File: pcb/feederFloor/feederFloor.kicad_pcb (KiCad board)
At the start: 2 copper layers, 13.4 x 31.1 mm, 7 parts, among them J1 IDC, J2 Conn_01x05_Female, U1 DS28E07

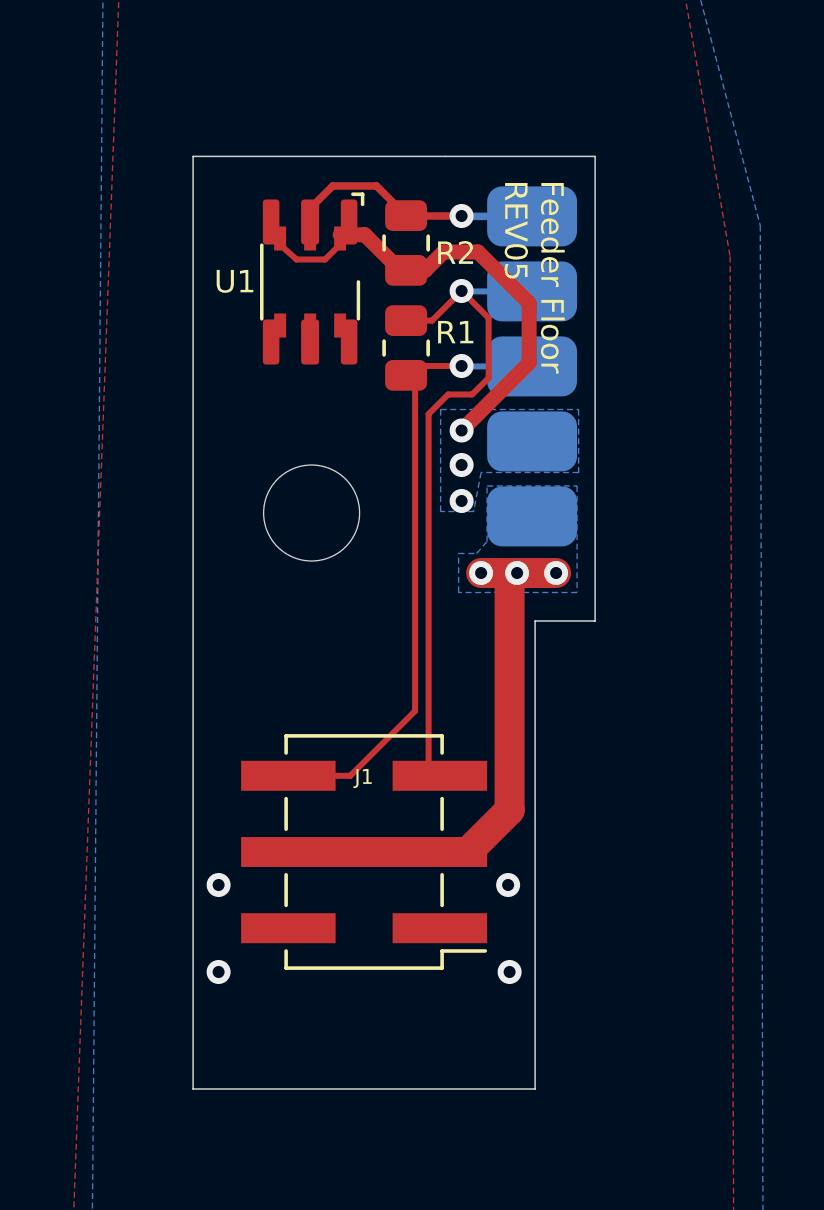
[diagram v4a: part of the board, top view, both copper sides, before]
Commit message: uprevs feederfloor to rev06, through hole IDC connector, adds silk for address, makes pads .1mm thinner, vdc has traces both sides
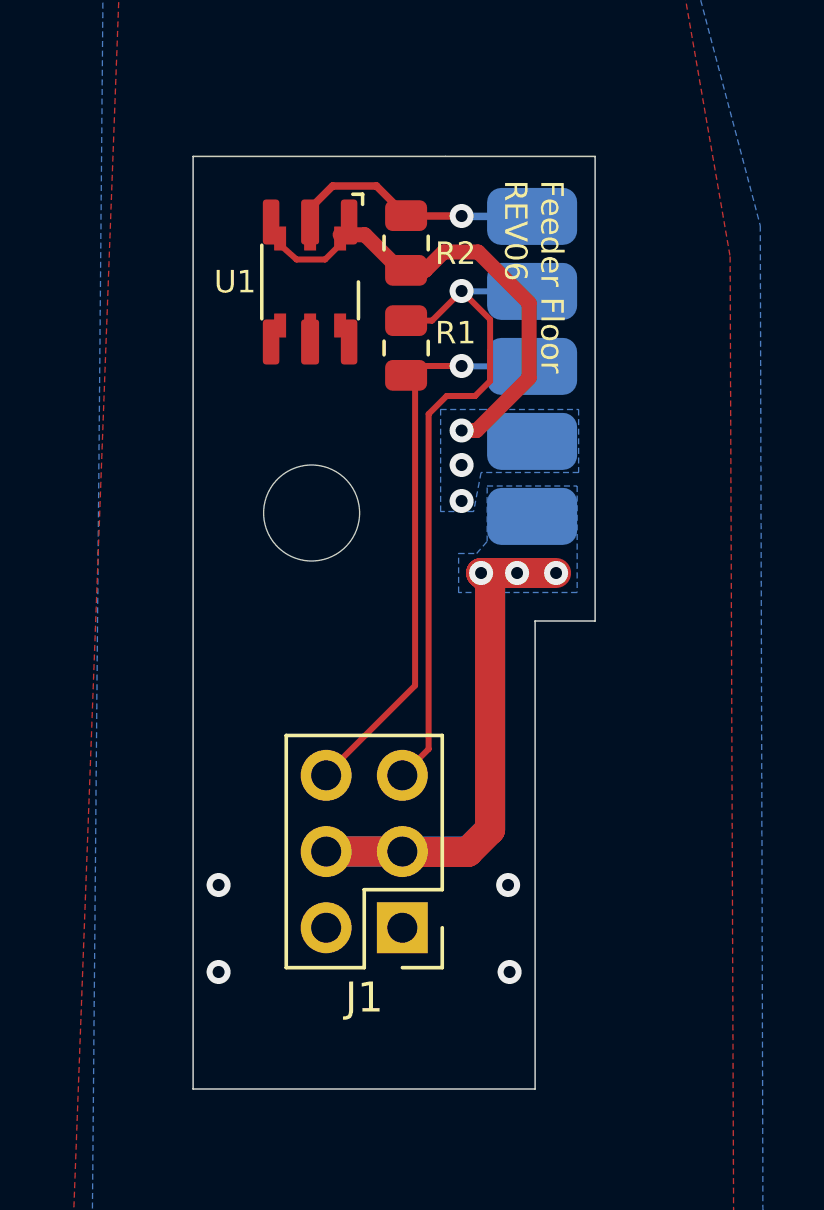
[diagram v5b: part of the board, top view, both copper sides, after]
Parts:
- removed G***: LOGO, index:logo
- J1: footprint Connector_PinHeader_2.54mm:PinHeader_2x03_P2.54mm_Vertical_SMD -> Connector_PinHeader_2.54mm:PinHeader_2x03_P2.54mm_Vertical
- moved J1 2.83 mm to (28.2, 50.8)
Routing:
- net VIN: track 18.5 -> 33.4 mm
- net RS-485-: track 20.8 -> 19.0 mm
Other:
- board text added: "50"
- board text added: "Feeder Floor REV06"
- board text removed: "Feeder Floor REV05"

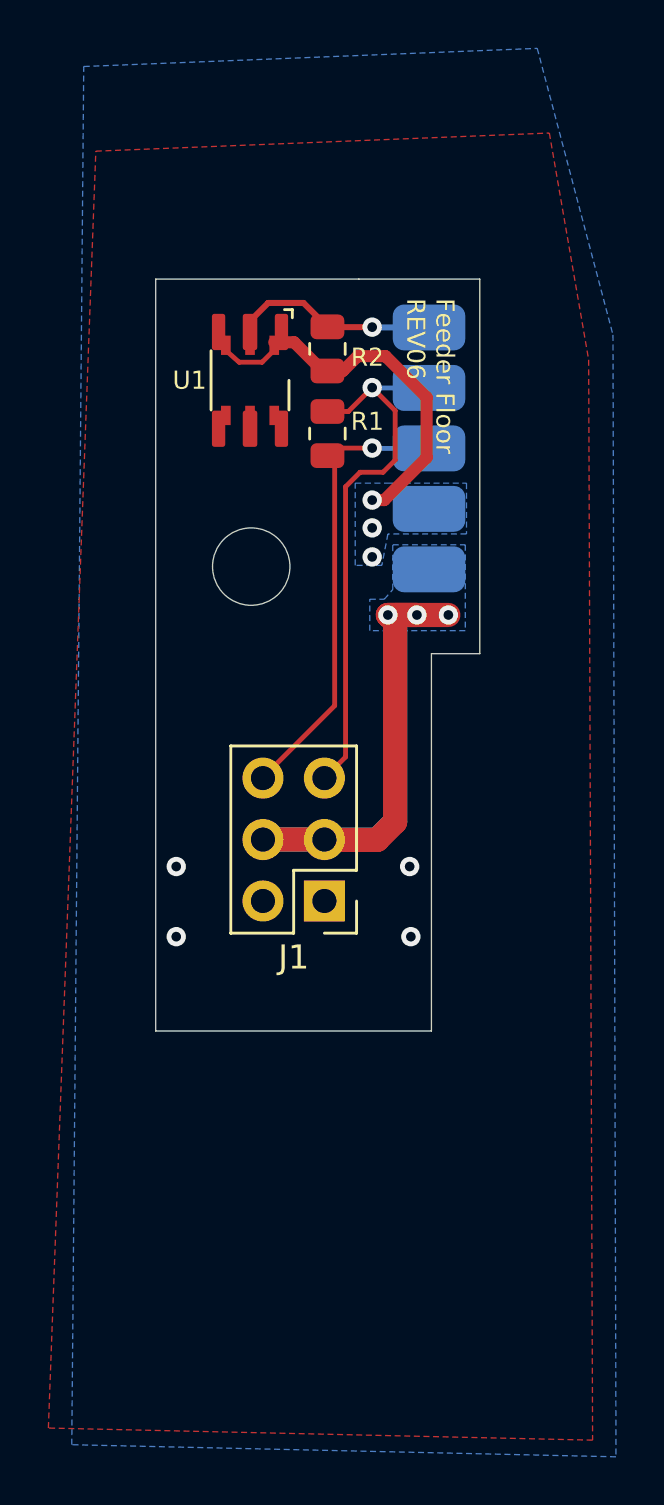
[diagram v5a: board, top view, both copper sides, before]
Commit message: updating fill zone outline of feeder floor to work with kikit
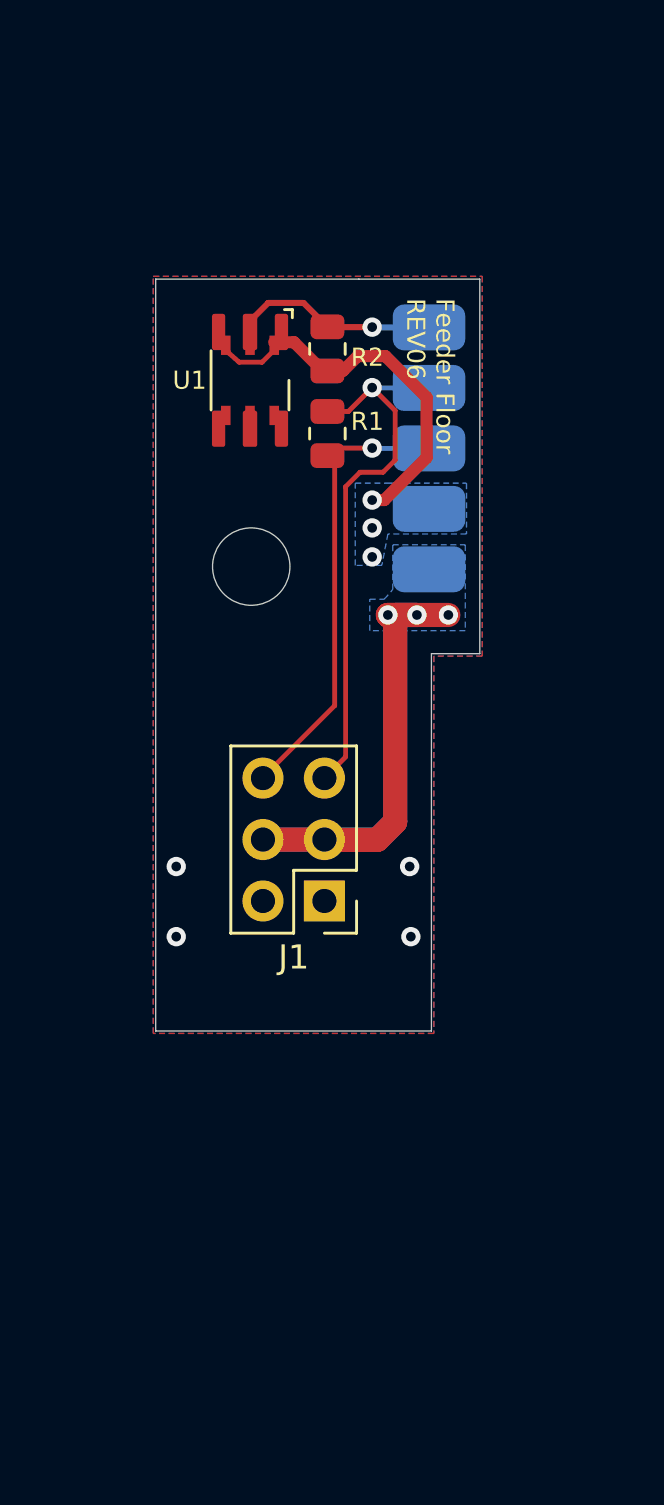
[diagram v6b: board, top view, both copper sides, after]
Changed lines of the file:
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@@
   (segment (start 30.2 32.1) (end 30.213687 32.113687) (width 0.2) (layer "B.Cu") (net 5))
   (segment (start 30.213687 32.113687) (end 32.550114 32.113687) (width 0.2) (layer "B.Cu") (net 5))
-  (zone (net 1) (net_name "GND") (layer "F.Cu") (hatch edge 0.508)
-    (connect_pads (clearance 0.3))
-    (min_thickness 0.2) (filled_areas_thickness no)
+  (zone (net 1) (net_name "GND") (layers F&B.Cu) (hatch edge 0.508)
+    (connect_pads (clearance 0.2))
+    (min_thickness 0.254) (filled_areas_thickness no)
     (fill yes (thermal_gap 0.508) (thermal_bridge_width 0.508))
     (polygon
       (pts
-        (xy 39.312982 73.115845)
-        (xy 16.812982 72.615845)
-        (xy 18.775 19.825)
-        (xy 37.525 19.075)
-        (xy 39.15 28.45)
+        (xy 34.75 40.7)
+        (xy 32.75 40.7)
+        (xy 32.75 56.3)
+        (xy 21.15 56.3)
+        (xy 21.15 25)
+        (xy 34.75 25)
       )
     )
-  )
-  (zone (net 1) (net_name "GND") (layer "B.Cu") (hatch edge 0.508)
-    (priority 11)
-    (connect_pads (clearance 0.25))
-    (min_thickness 0.2) (filled_areas_thickness no)
-    (fill yes (thermal_gap 0.508) (thermal_bridge_width 0.508))
-    (polygon
-      (pts
-        (xy 40.280398 73.804768)
-        (xy 17.780398 73.304768)
-        (xy 18.275 16.325)
-        (xy 37.025 15.575)
-        (xy 40.15562 27.419775)
-      )
-    )

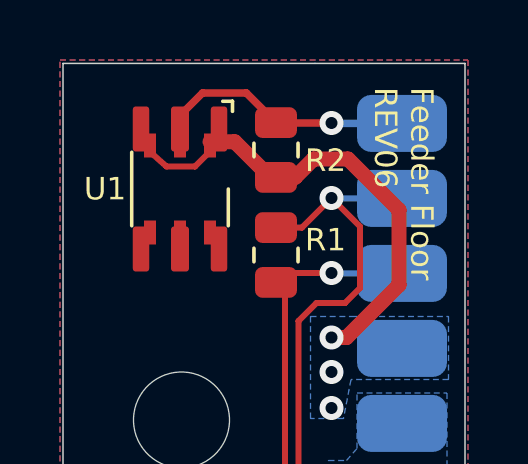
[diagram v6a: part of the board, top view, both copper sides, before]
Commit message: adds keepout copper for floor countersink. this commit represents rev07
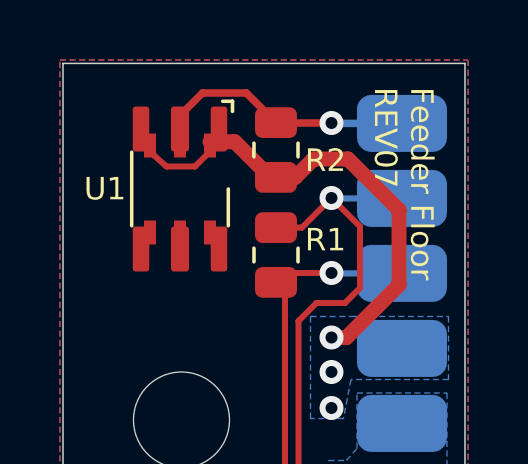
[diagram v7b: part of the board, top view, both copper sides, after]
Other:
- board text added: "Feeder Floor REV07"
- board text removed: "Feeder Floor REV06"
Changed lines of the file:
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@@
       (net 3 "VIN") (pinfunction "Pin_5") (pintype "passive"))
   )
-  (gr_circle (center 25.2 37) (end 22.2 37) (layer "B.SilkS") (width 0.12) (fill none))
+  (gr_circle (center 25.2 37) (end 22.25 37) (layer "B.SilkS") (width 0.12) (fill none))
+  (gr_circle (center 25.2 37) (end 28.5 37) (layer "Eco2.User") (width 0.2) (fill solid))
   (gr_line (start 32.650114 40.6) (end 32.65 56.2) (layer "Edge.Cuts") (width 0.05))
   (gr_line (start 34.650114 25.113687) (end 34.650114 40.6) (layer "Edge.Cuts") (width 0.05))
@@
     (effects (font (size 3 3) (thickness 0.5)) (justify mirror))
   )
-  (gr_text "Feeder Floor\nREV06" (at 32.6 25.9 270) (layer "F.SilkS")
+  (gr_text "Feeder Floor\nREV07" (at 32.6 25.9 270) (layer "F.SilkS")
     (effects (font (size 0.75 0.75) (thickness 0.1)) (justify left))
   )
